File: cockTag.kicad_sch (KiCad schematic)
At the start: 9 parts, among them J1 SWD, U1 KXTJ3-1057

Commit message: feat: Assign LCSC ids to the schematic
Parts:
- BT1: LCSC (none) -> C2902339
- C1, C2: LCSC C359190 -> C41851
- C3: LCSC (none) -> C5189830
- J1: footprint (none) -> Connector_PinHeader_1.27mm:PinHeader_1x04_P1.27mm_Vertical; LCSC (none) -> C2935944
- R1, R2: LCSC (none) -> C25940
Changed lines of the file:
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@@
       (effects (font (size 1.27 1.27)) hide)
     )
-    (property "LCSC" "C359190" (id 4) (at 77.47 85.09 0)
+    (property "LCSC" "C41851" (id 4) (at 77.47 85.09 0)
       (effects (font (size 1.27 1.27)) hide)
     )
@@
       (effects (font (size 1.27 1.27)) hide)
     )
-    (property "LCSC" "C359190" (id 4) (at 77.47 62.23 0)
+    (property "LCSC" "C41851" (id 4) (at 77.47 62.23 0)
       (effects (font (size 1.27 1.27)) hide)
     )
@@
       (effects (font (size 1.27 1.27)) hide)
     )
+    (property "LCSC" "C5189830" (id 4) (at 121.92 125.73 0)
+      (effects (font (size 1.27 1.27)) hide)
+    )
     (pin "1")
     (pin "2")
@@
     (property "Reference" "J1" (id 0) (at 161.29 117.602 0))
     (property "Value" "SWD" (id 1) (at 161.29 120.142 0))
-    (property "Footprint" "" (id 2) (at 161.29 127 0)
+    (property "Footprint" "Connector_PinHeader_1.27mm:PinHeader_1x04_P1.27mm_Vertical" (id 2) (at 161.29 127 0)
       (effects (font (size 1.27 1.27)) hide)
     )
     (property "Datasheet" "~" (id 3) (at 161.29 127 0)
+      (effects (font (size 1.27 1.27)) hide)
+    )
+    (property "LCSC" "C2935944" (id 4) (at 161.29 127 0)
       (effects (font (size 1.27 1.27)) hide)
     )
@@
       (effects (font (size 1.27 1.27)) hide)
     )
+    (property "LCSC" "C2902339" (id 4) (at 137.16 127 0)
+      (effects (font (size 1.27 1.27)) hide)
+    )
     (pin "1")
     (pin "2")
@@
       (effects (font (size 1.27 1.27)) hide)
     )
+    (property "LCSC" "C25940" (id 4) (at 128.27 63.5 0)
+      (effects (font (size 1.27 1.27)) hide)
+    )
     (pin "1")
     (pin "2")
@@
       (effects (font (size 1.27 1.27)) hide)
     )
+    (property "LCSC" "C25940" (id 4) (at 121.92 63.5 0)
+      (effects (font (size 1.27 1.27)) hide)
+    )

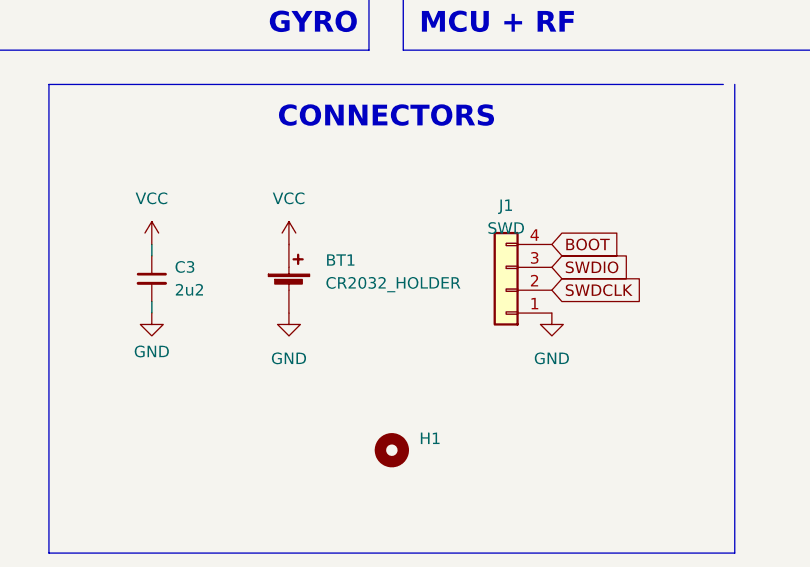
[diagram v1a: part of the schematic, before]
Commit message: Change CR2032 header LCSC id
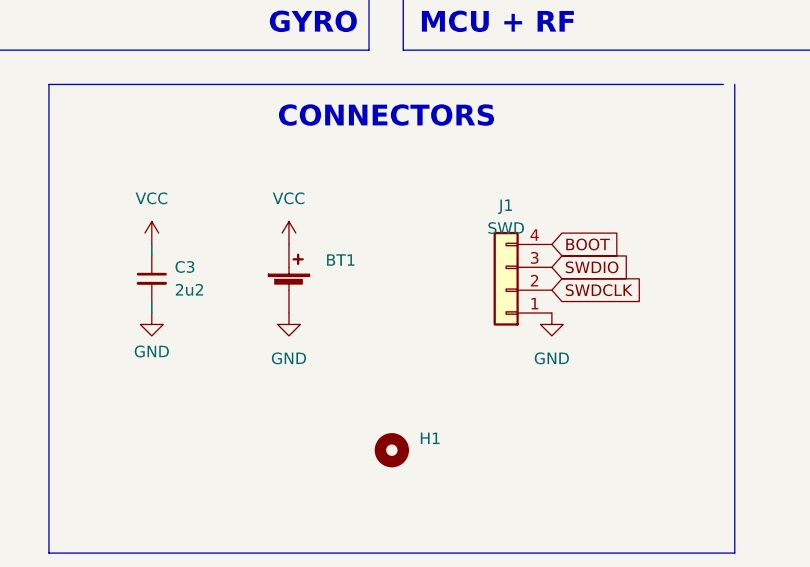
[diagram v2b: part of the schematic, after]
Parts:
- BT1: value CR2032_HOLDER -> (none); footprint Library:MY-2032-01 -> (none); LCSC C2902339 -> C964824
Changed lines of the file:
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@@
       (effects (font (size 1.27 1.27)) (justify left))
     )
-    (property "Value" "CR2032_HOLDER" (id 1) (at 141.224 126.2379 0)
+    (property "Value" "" (id 1) (at 141.224 126.2379 0)
       (effects (font (size 1.27 1.27)) (justify left))
     )
-    (property "Footprint" "Library:MY-2032-01" (id 2) (at 137.16 125.476 90)
+    (property "Footprint" "" (id 2) (at 137.16 125.476 90)
       (effects (font (size 1.27 1.27)) hide)
     )
@@
       (effects (font (size 1.27 1.27)) hide)
     )
-    (property "LCSC" "C2902339" (id 4) (at 137.16 127 0)
+    (property "LCSC" "C964824" (id 4) (at 137.16 127 0)
       (effects (font (size 1.27 1.27)) hide)
     )

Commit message: Change schematic to NRF52832
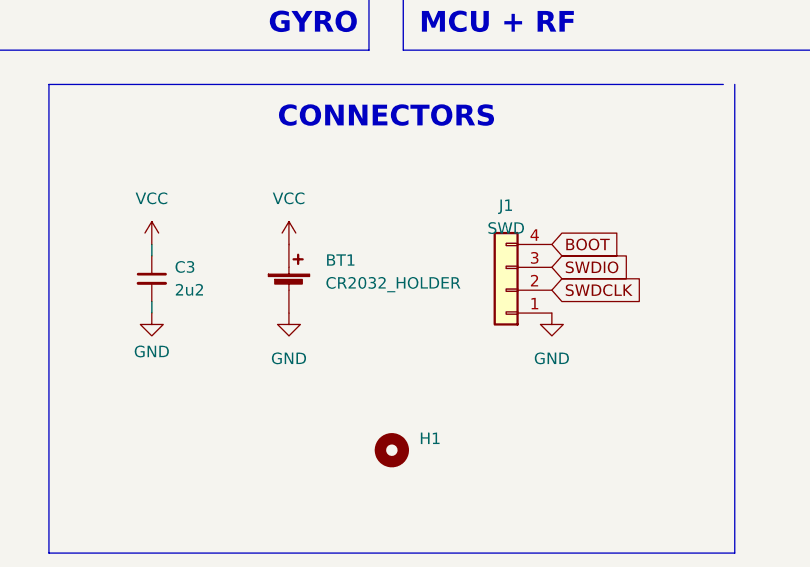
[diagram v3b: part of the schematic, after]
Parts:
- BT1: value (none) -> CR2032_HOLDER; footprint (none) -> Library:MY-2032-01
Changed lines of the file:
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@@
       (effects (font (size 1.27 1.27)) (justify left))
     )
-    (property "Value" "" (id 1) (at 141.224 126.2379 0)
-      (effects (font (size 1.27 1.27)) (justify left))
-    )
-    (property "Footprint" "" (id 2) (at 137.16 125.476 90)
+    (property "Value" "CR2032_HOLDER" (id 1) (at 141.224 126.2379 0)
+      (effects (font (size 1.27 1.27)) (justify left))
+    )
+    (property "Footprint" "Library:MY-2032-01" (id 2) (at 137.16 125.476 90)
       (effects (font (size 1.27 1.27)) hide)
     )
@@
       (reference "#PWR018") (unit 1) (value "VCC") (footprint "")
     )
-    (path "/b6ef546a-f2cf-48f2-a973-1f8e7a78bf18/adf5825b-05e2-4ba8-bbf2-4e31b380b4d6"
-      (reference "#PWR019") (unit 1) (value "VCC") (footprint "")
-    )
     (path "/b6ef546a-f2cf-48f2-a973-1f8e7a78bf18/eabf5d34-2e10-43dd-997f-461d6a3e3e54"
       (reference "#PWR020") (unit 1) (value "GND") (footprint "")
@@
       (reference "#PWR022") (unit 1) (value "GND") (footprint "")
     )
-    (path "/b6ef546a-f2cf-48f2-a973-1f8e7a78bf18/c1b28922-d556-474e-a19f-a0c855d01c01"
-      (reference "#PWR023") (unit 1) (value "GND") (footprint "")
-    )
-    (path "/b6ef546a-f2cf-48f2-a973-1f8e7a78bf18/b84e2630-486c-4a62-9351-f87c70f82b70"
-      (reference "#PWR024") (unit 1) (value "GND") (footprint "")
-    )
     (path "/b6ef546a-f2cf-48f2-a973-1f8e7a78bf18/8b48df41-a3f4-49d2-b565-f2f0405bfa96"
       (reference "#PWR025") (unit 1) (value "GND") (footprint "")
@@
       (reference "AE1") (unit 1) (value "2450AT18A100E") (footprint "RF_Antenna:Johanson_2450AT18x100")
     )
-    (path "/b6ef546a-f2cf-48f2-a973-1f8e7a78bf18/6db25935-f174-400a-9206-a98abcf213c2"
-      (reference "B1") (unit 1) (value "nRF-BALUN") (footprint "Library:FIL_2450BM14E0003T")
-    )
     (path "/ecf8d323-0ebc-4e00-ab52-4c41c91a2e5b"
       (reference "BT1") (unit 1) (value "CR2032_HOLDER") (footprint "Library:MY-2032-01")
@@
     )
     (path "/b6ef546a-f2cf-48f2-a973-1f8e7a78bf18/6335e93c-a32e-49c1-beda-01823bae59a1"
-      (reference "C4") (unit 1) (value "47n") (footprint "Capacitor_SMD:C_0402_1005Metric")
+      (reference "C4") (unit 1) (value "100p") (footprint "Capacitor_SMD:C_0402_1005Metric")
     )
     (path "/b6ef546a-f2cf-48f2-a973-1f8e7a78bf18/1b77f2ae-2811-4fa8-aec1-206e287b8b14"
@@
       (reference "C6") (unit 1) (value "1p") (footprint "Capacitor_SMD:C_0402_1005Metric")
     )
-    (path "/b6ef546a-f2cf-48f2-a973-1f8e7a78bf18/1d49e18d-e59f-4231-bfbf-880c88e3c3ec"
-      (reference "C7") (unit 1) (value "47n") (footprint "Capacitor_SMD:C_0402_1005Metric")
-    )
     (path "/b6ef546a-f2cf-48f2-a973-1f8e7a78bf18/34426879-3fbf-4507-8da5-57ea288b580f"
       (reference "C8") (unit 1) (value "12p") (footprint "Capacitor_SMD:C_0402_1005Metric")
@@
       (reference "C14") (unit 1) (value "1n") (footprint "Capacitor_SMD:C_0402_1005Metric")
     )
+    (path "/b6ef546a-f2cf-48f2-a973-1f8e7a78bf18/58510748-0bc0-4ee0-8b0c-b975cd1dbfe6"
+      (reference "C?") (unit 1) (value "1u") (footprint "Capacitor_SMD:C_0402_1005Metric")
+    )
+    (path "/b6ef546a-f2cf-48f2-a973-1f8e7a78bf18/9bc49620-4dce-4775-881f-f62ef11aa070"
+      (reference "C?") (unit 1) (value "100p") (footprint "Capacitor_SMD:C_0402_1005Metric")
+    )
     (path "/b6ef546a-f2cf-48f2-a973-1f8e7a78bf18/2ed370fa-93a3-4d09-aafa-1435208be822"
       (reference "D1") (unit 1) (value "LED") (footprint "LED_SMD:LED_0402_1005Metric")
@@
       (reference "U1") (unit 1) (value "KXTJ3-1057") (footprint "Package_LGA:Kionix_LGA-12_2x2mm_P0.5mm_LayoutBorder2x4y")
     )
-    (path "/b6ef546a-f2cf-48f2-a973-1f8e7a78bf18/93d7a44c-76ed-451b-9826-f85e91bfd260"
-      (reference "U2") (unit 1) (value "nRF51x22-QFxx") (footprint "Package_DFN_QFN:QFN-48-1EP_6x6mm_P0.4mm_EP4.6x4.6mm")
+    (path "/b6ef546a-f2cf-48f2-a973-1f8e7a78bf18/cc89fa23-a243-4555-89b5-e3868f114948"
+      (reference "U?") (unit 1) (value "nRF52832-QFxx") (footprint "Package_DFN_QFN:QFN-48-1EP_6x6mm_P0.4mm_EP4.6x4.6mm")
     )
     (path "/b6ef546a-f2cf-48f2-a973-1f8e7a78bf18/b89f102e-e954-4ae2-9e75-0ec3efd3cbc9"
